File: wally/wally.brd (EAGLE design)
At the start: 2 parts, among them IC1 ESP32-S3-WROOM-1-N4, U1 RA-01H

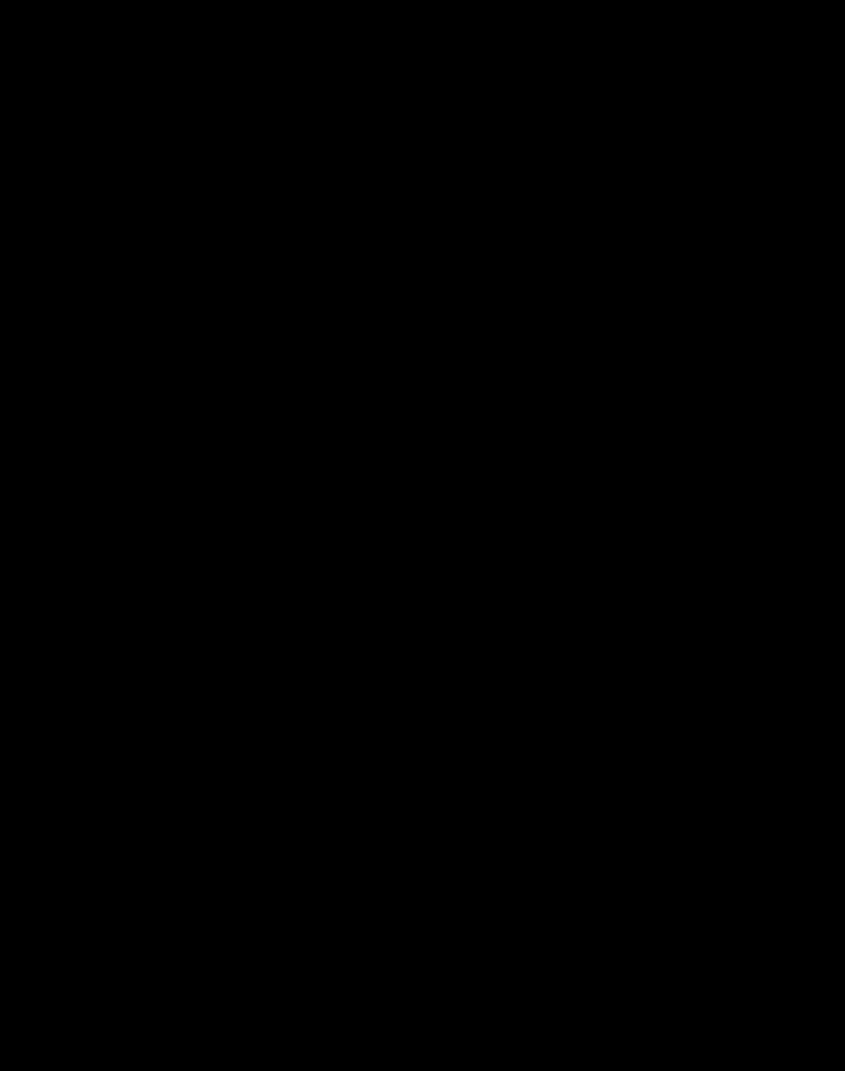
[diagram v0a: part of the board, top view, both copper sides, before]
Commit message: usb c port
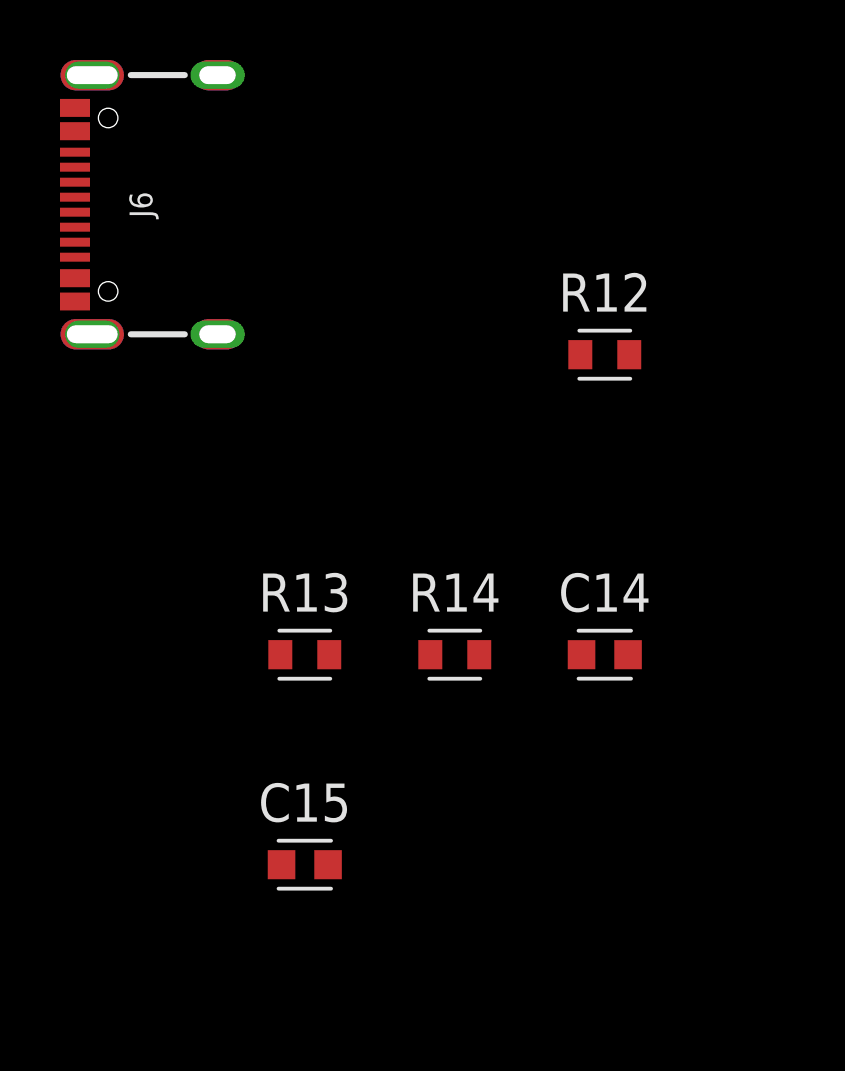
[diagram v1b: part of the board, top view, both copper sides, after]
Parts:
- added C14: 100n, Capacitor:CAPC1608X85
- added C15: 1u, Capacitor:CAPC1608X85
- added J6: USBC, SparkFun-Connectors:USB-C-16P-2LAYER-PADS
- added R12, R14: 5k1, Resistor:RESC1608X60
- added R13: 1M, Resistor:RESC1608X60
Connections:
- new net N$21: J6.SHLD1, J6.SHLD2, J6.SHLD3, J6.SHLD4, R13.1
- new net N$24: J6.B5, R12.1
- new net N$25: J6.A5, R14.1
- new net N$26: C14.2, C15.2
- new net USB_D+: J6.A6, J6.B6
- new net USB_D-: J6.A7, J6.B7
- net GND: now also C14.1, C15.1, J6.GND, J6.GND2, R12.2, R13.2, R14.2
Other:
- board outline added: 5 x 8.6 mm

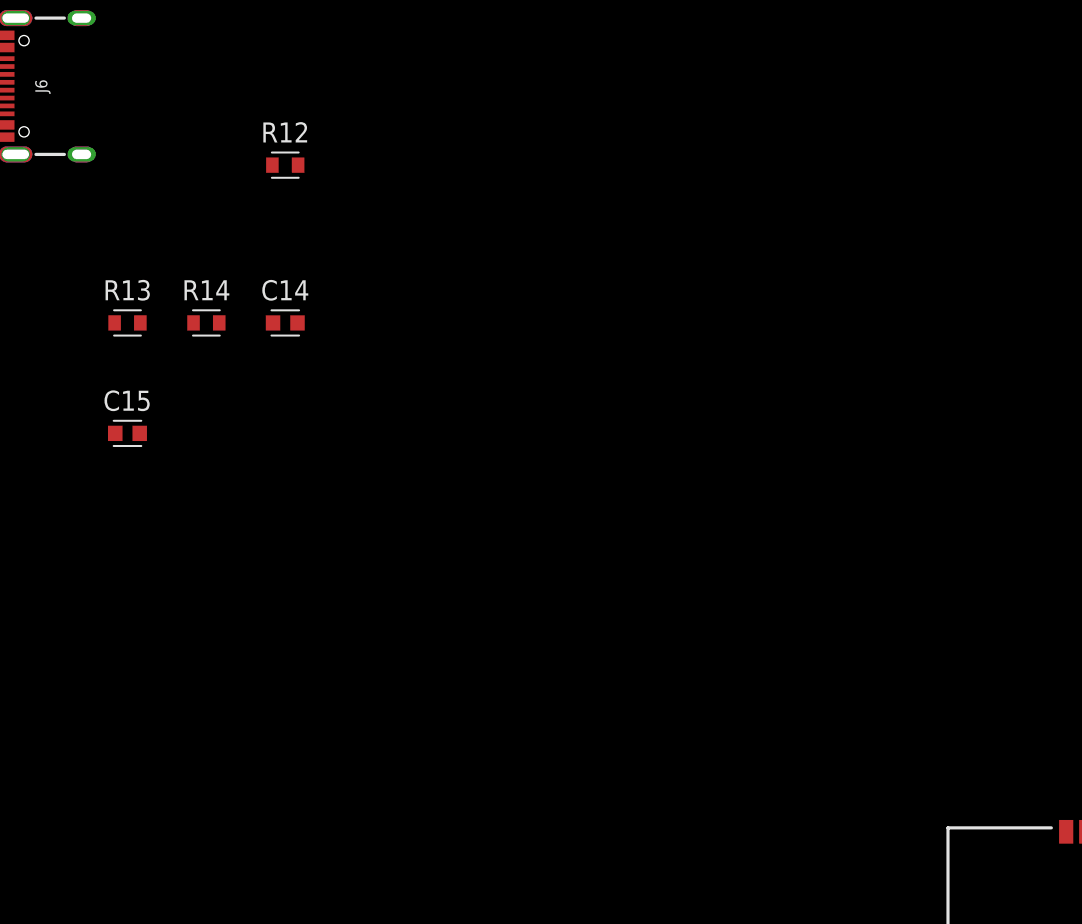
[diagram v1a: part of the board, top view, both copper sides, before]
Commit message: SIM7600G (treat as pin header)
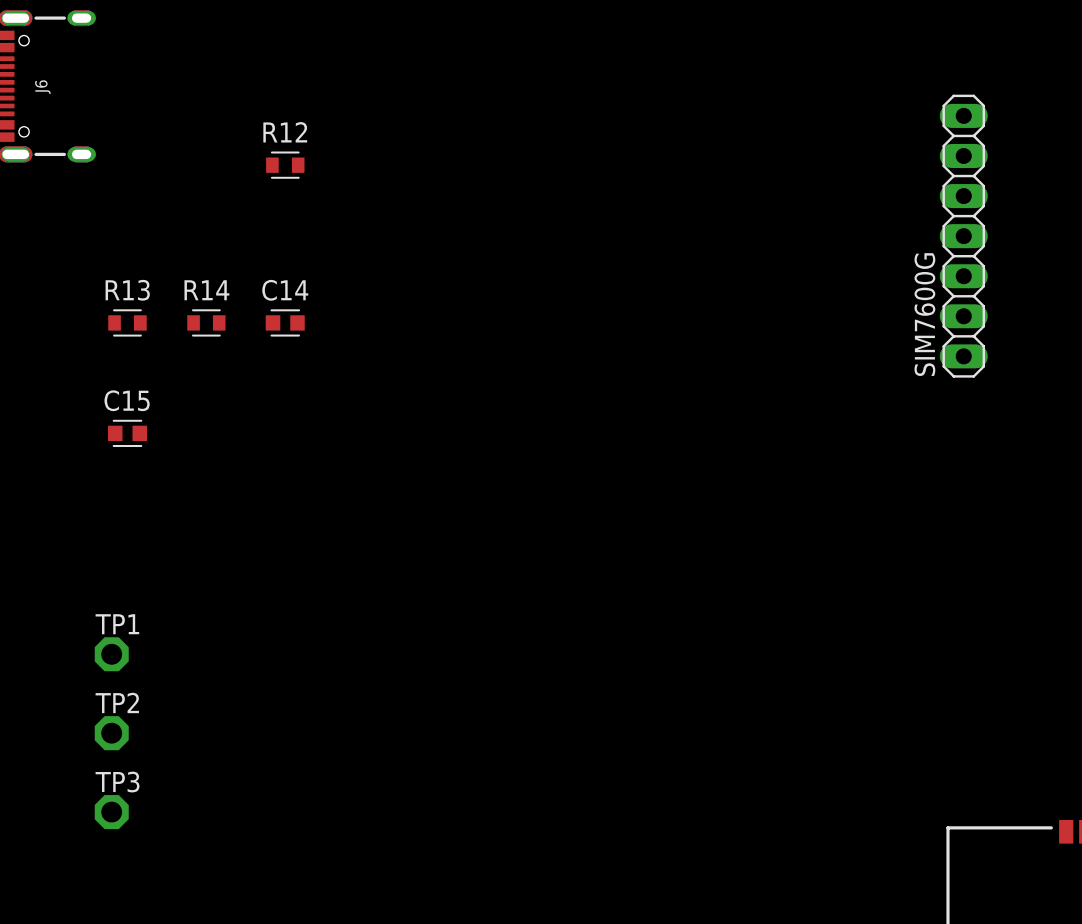
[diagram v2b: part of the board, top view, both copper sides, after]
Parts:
- added SIM7600G: PINHD-1X7, Connector:1X07
- added TP1, TP2, TP3: TPPAD1-13, testpad:P1-13
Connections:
- new net PWRKEY: SIM7600G.4, TP1.TP
- new net RXD: SIM7600G.2
- new net SLEEP: SIM7600G.7
- new net TXD: SIM7600G.3
- new net VSIM: SIM7600G.5, TP2.TP
- net GND: now also SIM7600G.1, SIM7600G.6, TP3.TP
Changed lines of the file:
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@@
 <attribute name="VOLTAGE_RATING" value="" x="-49" y="-65" size="1.778" layer="27" font="vector" ratio="15" display="off"/>
+</element>
+<element name="SIM7600G" library="Connector" library_urn="urn:adsk.eagle:library:16378166" package="1X07" package3d_urn="urn:adsk.eagle:package:22477/2" value="PINHD-1X7" x="3" y="-20.5" locked="yes" smashed="yes" rot="R90">
+<attribute name="CATEGORY" value="Headers" x="3" y="-20.5" locked="yes" size="1.778" layer="27" font="vector" ratio="15" rot="R90" display="off"/>
+<attribute name="DESCRIPTION" value="Header, Straight, 7 Position" x="3" y="-20.5" locked="yes" size="1.778" layer="27" font="vector" ratio="15" rot="R90" display="off"/>
+<attribute name="MANUFACTURER" value="Generic" x="3" y="-20.5" locked="yes" size="1.778" layer="27" font="vector" ratio="15" rot="R90" display="off"/>
+<attribute name="MPN" value="Generic" x="3" y="-20.5" locked="yes" size="1.778" layer="27" font="vector" ratio="15" rot="R90" display="off"/>
+<attribute name="NAME" x="1.1712" y="-29.4662" locked="yes" size="1.27" layer="25" ratio="10" rot="R90"/>
+<attribute name="OPERATING_TEMPERATURE" value="Generic" x="3" y="-20.5" locked="yes" size="1.778" layer="27" font="vector" ratio="15" rot="R90" display="off"/>
+<attribute name="PART_STATUS" value="Active" x="3" y="-20.5" locked="yes" size="1.778" layer="27" font="vector" ratio="15" rot="R90" display="off"/>
+<attribute name="PITCH" value="0.100&quot; (2.54mm)" x="3" y="-20.5" locked="yes" size="1.778" layer="27" font="vector" ratio="15" rot="R90" display="off"/>
+<attribute name="ROHS_COMPLIANCE" value="Generic" x="3" y="-20.5" locked="yes" size="1.778" layer="27" font="vector" ratio="15" rot="R90" display="off"/>
+<attribute name="SERIES" value="Generic" x="3" y="-20.5" locked="yes" size="1.778" layer="27" font="vector" ratio="15" rot="R90" display="off"/>
+<attribute name="SUB-CATEGORY" value="Headers, Male Pins" x="3" y="-20.5" locked="yes" size="1.778" layer="27" font="vector" ratio="15" rot="R90" display="off"/>
+<attribute name="TYPE" value="Board to Board or Cable, Unshrouded, Through Hole, Straight" x="3" y="-20.5" locked="yes" size="1.778" layer="27" font="vector" ratio="15" rot="R90" display="off"/>
+<attribute name="VALUE" x="6.175" y="-29.39" locked="yes" size="1.27" layer="27" rot="R90"/>
+</element>
+<element name="TP1" library="testpad" library_urn="urn:adsk.eagle:library:385" package="P1-13" package3d_urn="urn:adsk.eagle:package:27946/1" value="TPPAD1-13" x="-51" y="-47" smashed="yes">
+<attribute name="NAME" x="-52.016" y="-45.73" size="1.27" layer="25" ratio="10"/>
+<attribute name="POPULARITY" value="12" x="-51" y="-47" size="1.778" layer="27" font="vector" ratio="15" display="off"/>
+<attribute name="TP_SIGNAL_NAME" value="" x="-51" y="-47" size="1.778" layer="27" font="vector" ratio="15" display="off"/>
+<attribute name="VALUE" x="-51" y="-47" size="0.0254" layer="27"/>
+</element>
+<element name="TP2" library="testpad" library_urn="urn:adsk.eagle:library:385" package="P1-13" package3d_urn="urn:adsk.eagle:package:27946/1" value="TPPAD1-13" x="-51" y="-52" smashed="yes">
+<attribute name="NAME" x="-52.016" y="-50.73" size="1.27" layer="25" ratio="10"/>
+<attribute name="POPULARITY" value="12" x="-51" y="-52" size="1.778" layer="27" font="vector" ratio="15" display="off"/>
+<attribute name="TP_SIGNAL_NAME" value="" x="-51" y="-52" size="1.778" layer="27" font="vector" ratio="15" display="off"/>
+<attribute name="VALUE" x="-51" y="-52" size="0.0254" layer="27"/>
+</element>
+<element name="TP3" library="testpad" library_urn="urn:adsk.eagle:library:385" package="P1-13" package3d_urn="urn:adsk.eagle:package:27946/1" value="TPPAD1-13" x="-51" y="-57" smashed="yes">
+<attribute name="NAME" x="-52.016" y="-55.73" size="1.27" layer="25" ratio="10"/>
+<attribute name="POPULARITY" value="12" x="-51" y="-57" size="1.778" layer="27" font="vector" ratio="15" display="off"/>
+<attribute name="TP_SIGNAL_NAME" value="" x="-51" y="-57" size="1.778" layer="27" font="vector" ratio="15" display="off"/>
+<attribute name="VALUE" x="-51" y="-57" size="0.0254" layer="27"/>
 </element>
 </elements>
@@
 <contactref element="C15" pad="1"/>
 <contactref element="C14" pad="1"/>
-<wire x1="17" y1="-96.6821" x2="3" y2="-96.6821" width="0" layer="19" extent="1-1"/>
-<wire x1="15" y1="-81.3179" x2="17" y2="-96.6821" width="0" layer="19" extent="1-1"/>
-<wire x1="9.49" y1="-75.75" x2="15" y2="-81.3179" width="0" layer="19" extent="1-1"/>
-<wire x1="15.81" y1="-69.9" x2="9.49" y2="-75.75" width="0" layer="19" extent="1-1"/>
-<wire x1="17.21" y1="-69.9" x2="15.81" y2="-69.9" width="0" layer="19" extent="1-1"/>
-<wire x1="17.21" y1="-68.5" x2="17.21" y2="-69.9" width="0" layer="19" extent="1-1"/>
-<wire x1="17.21" y1="-67.1" x2="17.21" y2="-68.5" width="0" layer="19" extent="1-1"/>
-<wire x1="15.81" y1="-67.1" x2="17.21" y2="-67.1" width="0" layer="19" extent="1-1"/>
-<wire x1="15.81" y1="-68.5" x2="15.81" y2="-69.9" width="0" layer="19" extent="1-1"/>
+<contactref element="SIM7600G" pad="1"/>
+<contactref element="SIM7600G" pad="6"/>
+<contactref element="TP3" pad="TP"/>
+<wire x1="-50.7746" y1="-33" x2="-51" y2="-57" width="0" layer="19" extent="1-1"/>
+<wire x1="-49.1848" y1="-26" x2="-50.7746" y2="-33" width="0" layer="19" extent="1-1"/>
+<wire x1="-44.1848" y1="-26" x2="-49.1848" y2="-26" width="0" layer="19" extent="1-1"/>
+<wire x1="-40.7746" y1="-26" x2="-44.1848" y2="-26" width="0" layer="19" extent="1-1"/>
+<wire x1="-39.1848" y1="-16" x2="-40.7746" y2="-26" width="0" layer="19" extent="1-1"/>
+<wire x1="-57.66" y1="-14.225" x2="-49.1848" y2="-26" width="0" layer="19" extent="1-1"/>
+<wire x1="-57.66" y1="-7.775" x2="-57.66" y2="-14.225" width="0" layer="19" extent="1-1"/>
+<wire x1="3" y1="-15.42" x2="-39.1848" y2="-16" width="0" layer="19" extent="1-1"/>
+<wire x1="3" y1="-28.12" x2="3" y2="-15.42" width="0" layer="19" extent="1-1"/>
+<wire x1="9.49" y1="-58.25" x2="3" y2="-28.12" width="0" layer="19" extent="1-1"/>
+<wire x1="15.81" y1="-67.1" x2="9.49" y2="-58.25" width="0" layer="19" extent="1-1"/>
+<wire x1="17.21" y1="-67.1" x2="15.81" y2="-67.1" width="0" layer="19" extent="1-1"/>
+<wire x1="17.21" y1="-68.5" x2="17.21" y2="-67.1" width="0" layer="19" extent="1-1"/>
+<wire x1="17.21" y1="-69.9" x2="17.21" y2="-68.5" width="0" layer="19" extent="1-1"/>
+<wire x1="15.81" y1="-69.9" x2="17.21" y2="-69.9" width="0" layer="19" extent="1-1"/>
+<wire x1="15.81" y1="-68.5" x2="15.81" y2="-67.1" width="0" layer="19" extent="1-1"/>
 <wire x1="18.61" y1="-69.9" x2="17.21" y2="-69.9" width="0" layer="19" extent="1-1"/>
 <wire x1="18.61" y1="-68.5" x2="17.21" y2="-68.5" width="0" layer="19" extent="1-1"/>
 <wire x1="18.61" y1="-67.1" x2="17.21" y2="-67.1" width="0" layer="19" extent="1-1"/>
-<wire x1="9.49" y1="-58.25" x2="15.81" y2="-67.1" width="0" layer="19" extent="1-1"/>
-<wire x1="-40.7746" y1="-26" x2="9.49" y2="-58.25" width="0" layer="19" extent="1-1"/>
-<wire x1="-44.1848" y1="-26" x2="-40.7746" y2="-26" width="0" layer="19" extent="1-1"/>
-<wire x1="-49.1848" y1="-26" x2="-44.1848" y2="-26" width="0" layer="19" extent="1-1"/>
-<wire x1="-50.7746" y1="-33" x2="-49.1848" y2="-26" width="0" layer="19" extent="1-1"/>
-<wire x1="-39.1848" y1="-16" x2="-40.7746" y2="-26" width="0" layer="19" extent="1-1"/>
-<wire x1="-57.66" y1="-14.225" x2="-49.1848" y2="-26" width="0" layer="19" extent="1-1"/>
-<wire x1="-57.66" y1="-7.775" x2="-57.66" y2="-14.225" width="0" layer="19" extent="1-1"/>
+<wire x1="9.49" y1="-75.75" x2="15.81" y2="-69.9" width="0" layer="19" extent="1-1"/>
+<wire x1="15" y1="-81.3179" x2="9.49" y2="-75.75" width="0" layer="19" extent="1-1"/>
+<wire x1="17" y1="-96.6821" x2="15" y2="-81.3179" width="0" layer="19" extent="1-1"/>
+<wire x1="3" y1="-96.6821" x2="17" y2="-96.6821" width="0" layer="19" extent="1-1"/>
 </signal>
 <signal name="3V3">
@@
 <wire x1="-57.66" y1="-10.75" x2="-57.66" y2="-11.75" width="0" layer="19" extent="1-1"/>
 </signal>
+<signal name="RXD">
+<contactref element="SIM7600G" pad="2"/>
+</signal>
+<signal name="TXD">
+<contactref element="SIM7600G" pad="3"/>
+</signal>
+<signal name="PWRKEY">
+<contactref element="SIM7600G" pad="4"/>
+<contactref element="TP1" pad="TP"/>
+<wire x1="3" y1="-20.5" x2="-51" y2="-47" width="0" layer="19" extent="1-1"/>
+</signal>
+<signal name="VSIM">
+<contactref element="SIM7600G" pad="5"/>
+<contactref element="TP2" pad="TP"/>
+<wire x1="3" y1="-17.96" x2="-51" y2="-52" width="0" layer="19" extent="1-1"/>
+</signal>
+<signal name="SLEEP">
+<contactref element="SIM7600G" pad="7"/>
+</signal>
 </signals>

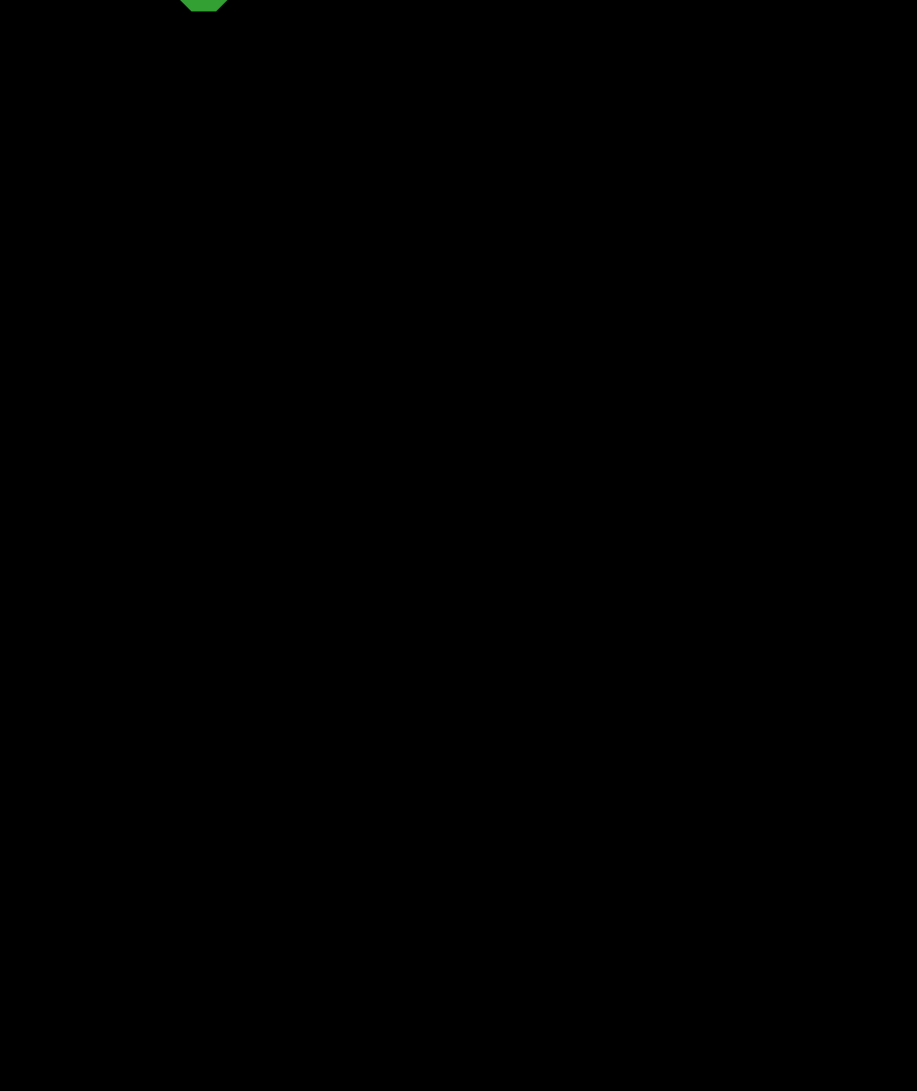
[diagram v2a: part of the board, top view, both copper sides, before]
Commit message: Boost circuit for SIM
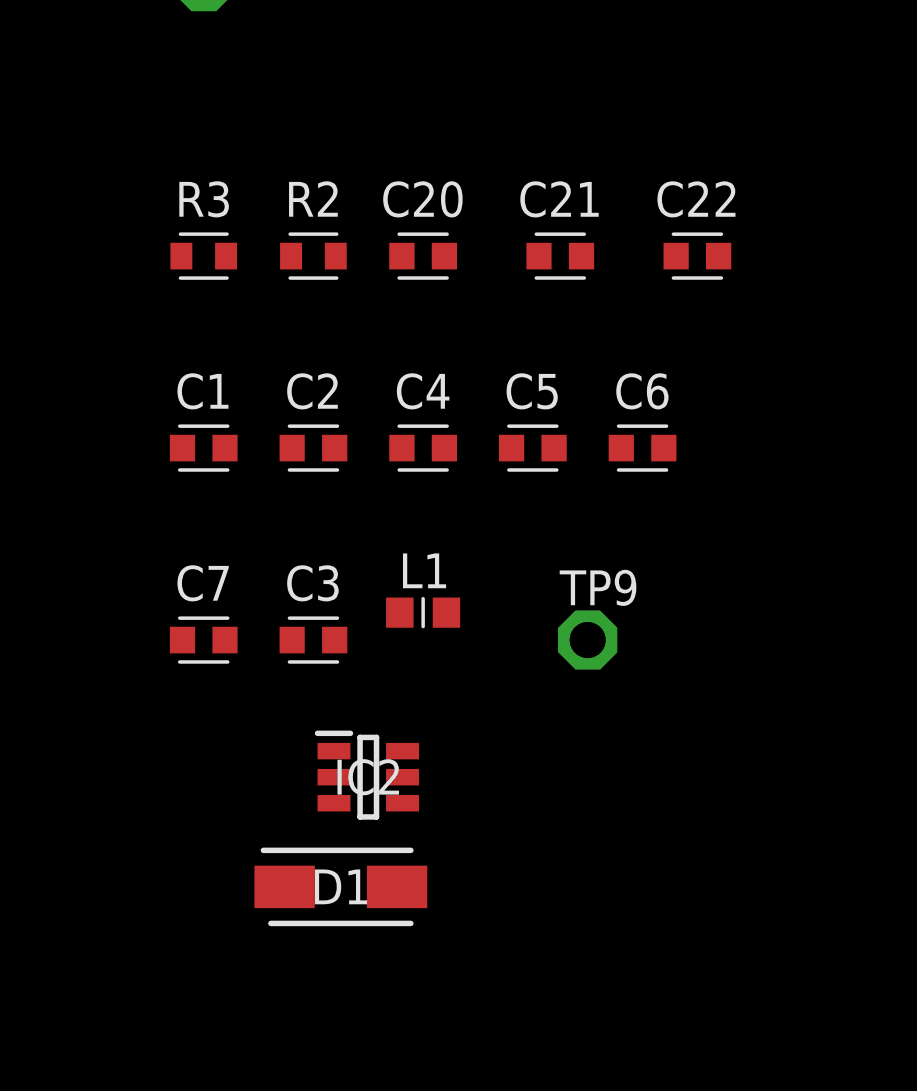
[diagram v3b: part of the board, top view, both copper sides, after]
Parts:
- added C1, C2: 10u, Capacitor:CAPC1608X85
- added C20, C21, C22, C4, C5, C6, C7: 22u, Capacitor:CAPC1608X85
- added C3: 1u, Capacitor:CAPC1608X85
- added D1: SSA34-E3_5AT, SamacSys_Parts:DIOM5127X229N
- added IC2: XTLV61048DBVR, SamacSys_Parts:SOT95P280X145-6N
- added L1: 10uH, BeagleBone_Blue_R3:L0603
- added R2: 1M, Resistor:RESC1608X60
- added R3: 120k, Resistor:RESC1608X60
- added TP9: PTR1PAD1-13, testpad:P1-13
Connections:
- new net N$2: C3.1, D1.2, IC2.1, L1.1
- new net N$3: IC2.3, R2.2, R3.1
- new net VCC: C1.1, C20.2, C21.2, C22.2, C4.2, C5.2, C6.2, C7.2, IC2.4, IC2.5, L1.2
- net GND: now also C1.2, C2.1, C20.1, C21.1, C22.1, C3.2, C4.1, C5.1, C6.1, C7.1, IC2.2, IC2.6, R3.2
- net VSIM: now also C2.2, D1.1, R2.1, TP9.TP
